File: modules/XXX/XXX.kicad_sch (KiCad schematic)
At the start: 15 parts, among them J1 CardConnector, SW1 AS13AP, SW2 AS13AP, SW3 AS13AP

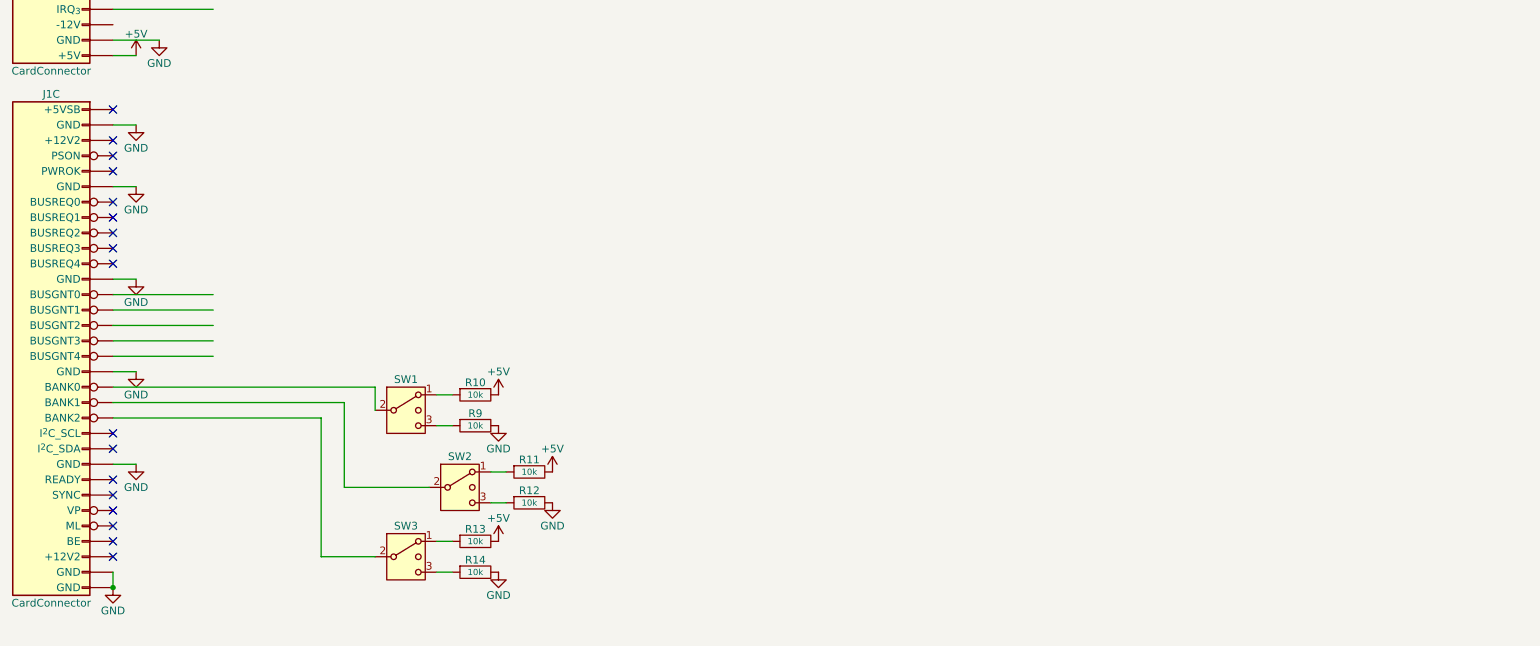
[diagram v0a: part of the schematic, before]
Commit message: fixed level shifter footprint width
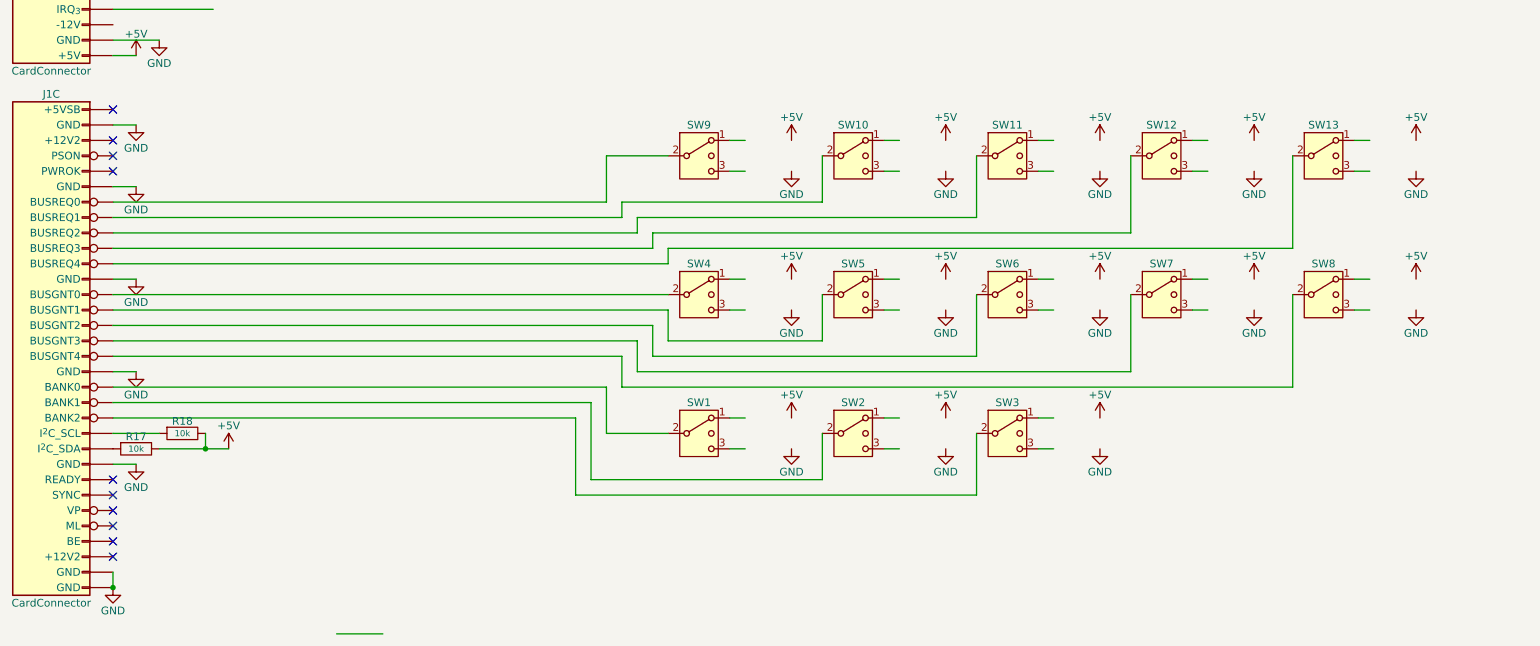
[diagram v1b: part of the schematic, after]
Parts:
- removed R10, R11, R12, R13, R14, R9: 10k, IMNOTWOPR:R_Axial_DIN0207_P400mil, symbol IMNOTWOPR:R_Horizontal
- added R17, R18: 10k, IMNOTWOPR:R_Axial_DIN0207_P400mil, symbol IMNOTWOPR:R_Horizontal
- added SW10, SW11, SW12, SW13, SW4, SW5, SW6, SW7, SW8, SW9: AS13AP, IMNOTWOPR:AS13AP, symbol Switch:SW_SPDT_MSM
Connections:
- net +5V: now also R17.2, R18.2
- net at J1.c10 (BUSREQ3): now also SW12.2 (3)
- net at J1.c11 (BUSREQ4): now also SW13.2 (3)
- net at J1.c13 (BUSGNT0): now also SW4.2 (3)
- net at J1.c14 (BUSGNT1): now also SW5.2 (3)
- net at J1.c15 (BUSGNT2): now also SW6.2 (3)
- net at J1.c16 (BUSGNT3): now also SW7.2 (3)
- net at J1.c17 (BUSGNT4): now also SW8.2 (3)
- net at J1.c22 (I^{2}C_SCL): now also R18.1
- net at J1.c23 (I^{2}C_SDA): now also R17.1
- net at J1.c7 (BUSREQ0): now also SW9.2 (3)
- net at J1.c8 (BUSREQ1): now also SW10.2 (3)
- net at J1.c9 (BUSREQ2): now also SW11.2 (3)
- no-connect marks 29 -> 22
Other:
- moved on the sheet: SW1, SW2, SW3

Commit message: xxx bus terminator card
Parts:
- removed R17, R18: 10k, IMNOTWOPR:R_Axial_DIN0207_P400mil, symbol IMNOTWOPR:R_Horizontal
- removed RN4: 10k, Resistor_THT:R_Array_SIP9, symbol Device:R_Network08
- removed SW1, SW2, SW3, SW4, SW5, SW6, SW7, SW8: AS13AP, IMNOTWOPR:AS13AP, symbol Switch:SW_SPDT_MSM
- added JP1: SDA_PU, IMNOTWOPR:Jumper_1x02, symbol Jumper:Jumper_2_Bridged
- added JP2: SCL_PU, IMNOTWOPR:Jumper_1x02, symbol Jumper:Jumper_2_Bridged
- added R1, R2: 4k7, IMNOTWOPR:R_Axial_DIN0207_P400mil, symbol IMNOTWOPR:R_Vertical
- added R3, R4: 1k, IMNOTWOPR:R_Axial_DIN0207_P400mil, symbol IMNOTWOPR:R_Vertical
- added R5, R6, R7: 47k, IMNOTWOPR:R_Axial_DIN0207_P400mil, symbol IMNOTWOPR:R_Vertical
- added RN6, RN7, RN8: 47k, Resistor_THT:R_Array_SIP6, symbol Device:R_Network05
- RN1: value 10k -> 47k
- RN3: value 10k -> 4k7
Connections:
- net +5V: now also RN1.1 (common), RN2.1 (common), JP1.2 (B), JP2.2 (B), R3.2, R4.2, R5.2, R6.2, R7.2, RN6.1 (common), RN7.1 (common), RN8.1 (common)
- net GND: now also RN3.1 (common)
- net at J1.b10 (A_{6}): no longer RN3.8 (R7)
- net at J1.b11 (A_{7}): no longer RN3.9 (R8)
- net #RESET: now reaches J1.b12 (RESET)
- net #RESET: now also RN6.2 (R1)
- net #IRQ: now reaches J1.b24 (IRQ)
- net #IRQ: now also RN6.4 (R3)
- net #NMI: now reaches J1.b25 (NMI)
- net #NMI: now also RN6.5 (R4)
- net #IRQ0: now reaches J1.b26 (IRQ_{0})
- net #IRQ0: now also RN1.2 (R1)
- net #IRQ1: now reaches J1.b27 (IRQ_{1})
- net #IRQ1: now also RN1.4 (R3)
- net #IRQ2: now reaches J1.b28 (IRQ_{2})
- net #IRQ2: now also RN1.6 (R5)
- net #IRQ3: now reaches J1.b29 (IRQ_{3})
- net #IRQ3: now also RN1.8 (R7)
- net at J1.b4 (A_{0}): no longer RN3.2 (R1)
- net at J1.b5 (A_{1}): no longer RN3.3 (R2)
- net at J1.b6 (A_{2}): no longer RN3.4 (R3)
- net at J1.b7 (A_{3}): no longer RN3.5 (R4)
- net at J1.b8 (A_{4}): no longer RN3.6 (R5)
- net at J1.b9 (A_{5}): no longer RN3.7 (R6)
- net #BANK1: now reaches J1.c20 (BANK1)
- net #BANK1: now also R6.1
- net #BUSGNT1: now reaches J1.c14 (BUSGNT1)
- net #BUSGNT1: now also RN8.3 (R2)
- net at J1.a4 (A_{8}): no longer RN1.2 (R1)
- net at J1.a5 (A_{9}): no longer RN1.3 (R2)
- net at J1.a6 (A_{10}): no longer RN1.4 (R3)
- net at J1.a7 (A_{11}): no longer RN1.5 (R4)
- net at J1.a8 (A_{12}): no longer RN1.6 (R5)
- net at J1.a9 (A_{13}): no longer RN1.7 (R6)
- net at J1.a10 (A_{14}): no longer RN1.8 (R7)
- net at J1.a11 (A_{15}): no longer RN1.9 (R8)
- net #BUSGNT4: now reaches J1.c17 (BUSGNT4)
- net #BUSGNT4: now also RN8.6 (R5)
- net at J1.a12 (A_{16}): no longer RN2.2 (R1)
- net at J1.a13 (A_{17}): no longer RN2.3 (R2)
- net at J1.a14 (A_{18}): no longer RN2.4 (R3)
- net at J1.a15 (A_{19}): no longer RN2.5 (R4)
- net at J1.a16 (A_{20}): no longer RN2.6 (R5)
- net at J1.a17 (A_{21}): no longer RN2.7 (R6)
- net at J1.a18 (A_{22}): no longer RN2.8 (R7)
- net at J1.a19 (A_{23}): no longer RN2.9 (R8)
- net #ABORT: now reaches J1.a20 (ABORT)
- net #ABORT: now also RN6.3 (R2)
- net #HALT: now reaches J1.a25 (HALT?)
- net #HALT: now also RN6.6 (R5)
- net #IRQ4: now reaches J1.a26 (IRQ_{4})
- net #IRQ4: now also RN1.3 (R2)
- net #IRQ5: now reaches J1.a27 (IRQ_{5})
- net #IRQ5: now also RN1.5 (R4)
- net #IRQ6: now reaches J1.a28 (IRQ_{6})
- net #IRQ6: now also RN1.7 (R6)
- net #IRQ7: now reaches J1.a29 (IRQ_{7})
- net #IRQ7: now also RN1.9 (R8)
- net #BUSGNT0: now reaches J1.c13 (BUSGNT0)
- net #BUSGNT0: now also RN8.2 (R1)
- net at SW12.2 (3): no longer J1.c10 (BUSREQ3)
- net at SW10.2 (3): no longer J1.c8 (BUSREQ1)
- net at J1.c22 (I^{2}C_SCL): now also R2.1
- net at SW13.2 (3): no longer J1.c11 (BUSREQ4)
- net at J1.c23 (I^{2}C_SDA): now also R1.1
- net #BANK2: now reaches J1.c21 (BANK2)
- net #BANK2: now also R7.1
- net #BUSGNT2: now reaches J1.c15 (BUSGNT2)
- net #BUSGNT2: now also RN8.4 (R3)
- net at SW11.2 (3): no longer J1.c9 (BUSREQ2)
- net #BANK0: now reaches J1.c19 (BANK0)
- net #BANK0: now also R5.1
- net #BUSGNT3: now reaches J1.c16 (BUSGNT3)
- net #BUSGNT3: now also RN8.5 (R4)
- net READY: now reaches J1.c25 (READY)
- net READY: now also R3.1
- net BE: now reaches J1.c29 (BE)
- net BE: now also R4.1
- net at SW9.2 (3): no longer J1.c7 (BUSREQ0)
- new net: JP2.1 (A), R2.2
- new net: JP1.1 (A), R1.2
- new net #BUSREQ0: J1.c7 (BUSREQ0), RN7.2 (R1)
- new net #BUSREQ1: J1.c8 (BUSREQ1), RN7.3 (R2)
- new net #BUSREQ2: J1.c9 (BUSREQ2), RN7.4 (R3)
- new net #BUSREQ3: J1.c10 (BUSREQ3), RN7.5 (R4)
- new net #BUSREQ4: J1.c11 (BUSREQ4), RN7.6 (R5)
- no-connect marks 22 -> 48
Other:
- note added: "BUS BIAS"
- moved on the sheet: SW10, SW11, SW12, SW13, SW9

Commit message: pxx prototype card
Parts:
- removed SW10, SW11, SW12, SW13, SW9: AS13AP, IMNOTWOPR:AS13AP, symbol Switch:SW_SPDT_MSM
- added SW1, SW2, SW3, SW4, SW5, SW6, SW7, SW8: SW_SPDT_MSM, IMNOTWOPR:AS13AP, symbol IMNOTWOPR:SW_SPDT_MSM
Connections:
- net #BANK0: now also SW1.2 (3)
- net #BANK1: now also SW2.2 (3)
- net #BANK2: now also SW3.2 (3)
- net #BUSGNT0: now also SW4.2 (3)
- net #BUSGNT1: now also SW5.2 (3)
- net #BUSGNT2: now also SW6.2 (3)
- net #BUSGNT3: now also SW7.2 (3)
- net #BUSGNT4: now also SW8.2 (3)
- net at RN2.2 (R1): now also SW1.1
- net at RN2.3 (R2): now also SW2.1
- net at RN2.4 (R3): now also SW3.1
- net at RN2.5 (R4): now also SW4.1
- net at RN2.6 (R5): now also SW5.1
- net at RN2.7 (R6): now also SW6.1
- net at RN2.8 (R7): now also SW7.1
- net at RN2.9 (R8): now also SW8.1
- net at RN3.2 (R1): now also SW1.3 (4)
- net at RN3.3 (R2): now also SW2.3 (4)
- net at RN3.4 (R3): now also SW3.3 (4)
- net at RN3.5 (R4): now also SW4.3 (4)
- net at RN3.6 (R5): now also SW5.3 (4)
- net at RN3.7 (R6): now also SW6.3 (4)
- net at RN3.8 (R7): now also SW7.3 (4)
- net at RN3.9 (R8): now also SW8.3 (4)
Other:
- moved on the sheet: RN2, RN3

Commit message: work on RAM and bus terminator
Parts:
- removed RN2: 10k, Resistor_THT:R_Array_SIP9, symbol Device:R_Network08
- removed RN3: 4k7, Resistor_THT:R_Array_SIP9, symbol Device:R_Network08
- added R10, R11, R12, R13, R14, R15, R8, R9: 10k, IMNOTWOPR:R_Axial_DIN0207_P400mil, symbol IMNOTWOPR:R_Vertical
- added R16, R17, R18, R19, R20, R21, R22, R23: 4k7, IMNOTWOPR:R_Axial_DIN0207_P400mil, symbol IMNOTWOPR:R_Vertical
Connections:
- net +5V: now also R10.2, R11.2, R12.2, R13.2, R14.2, R15.2, R8.2, R9.2
- net GND: now also R16.2, R17.2, R18.2, R19.2, R20.2, R21.2, R22.2, R23.2
- net at SW2.1: now also R9.1
- net at SW2.3 (4): now also R17.1
- net at SW6.1: now also R13.1
- net at SW6.3 (4): now also R21.1
- net at SW1.1: now also R8.1
- net at SW1.3 (4): now also R16.1
- net at SW4.1: now also R11.1
- net at SW4.3 (4): now also R19.1
- net at SW3.1: now also R10.1
- net at SW5.1: now also R12.1
- net at SW7.1: now also R14.1
- net at SW8.1: now also R15.1
- net at SW7.3 (4): now also R22.1
- net at SW5.3 (4): now also R20.1
- net at SW3.3 (4): now also R18.1
- net at SW8.3 (4): now also R23.1

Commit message: terminator card work
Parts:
- removed RN1: 47k, Resistor_THT:R_Array_SIP9, symbol Device:R_Network08
- removed RN6, RN7, RN8: 47k, Resistor_THT:R_Array_SIP6, symbol Device:R_Network05
- added R24, R25, R26, R27, R28, R29, R30, R31, R32, R33, R34, R35, R36, R37, R38, R39, R40, R41, R42, R43, R44, R45, R46: 47k, IMNOTWOPR:R_Axial_DIN0207_P400mil, symbol IMNOTWOPR:R_Vertical
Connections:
- net #ABORT: now also R25.1
- net #BUSGNT0: now also R42.1
- net #BUSGNT1: now also R43.1
- net #BUSGNT2: now also R44.1
- net #BUSGNT3: now also R45.1
- net #BUSGNT4: now also R46.1
- net #BUSREQ0: now also R37.1
- net #BUSREQ1: now also R38.1
- net #BUSREQ2: now also R39.1
- net #BUSREQ3: now also R40.1
- net #BUSREQ4: now also R41.1
- net #HALT: now also R28.1
- net #IRQ: now also R26.1
- net #IRQ0: now also R29.1
- net #IRQ1: now also R31.1
- net #IRQ2: now also R33.1
- net #IRQ3: now also R35.1
- net #IRQ4: now also R30.1
- net #IRQ5: now also R32.1
- net #IRQ6: now also R34.1
- net #IRQ7: now also R36.1
- net #NMI: now also R27.1
- net #RESET: now also R24.1
- net +5V: now also R24.2, R25.2, R26.2, R27.2, R28.2, R29.2, R30.2, R31.2, R32.2, R33.2, R34.2, R35.2, R36.2, R37.2, R38.2, R39.2, R40.2, R41.2, R42.2, R43.2, R44.2, R45.2, R46.2
- net +12V: no longer names the net of J1.a3 (+12V)
- net +12V: no longer J1.a30 (+12V)
- net -12V: no longer names the net of J1.b3 (-12V)
- no-connect marks 48 -> 51
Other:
- moved on the sheet: R10, R11, R12, R13, R14, R15, R16, R17, R18, R19, R20, R21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
